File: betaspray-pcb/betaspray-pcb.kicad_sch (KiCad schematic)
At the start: 1 part, among them U1 ESP32-S3

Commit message: Add LDO
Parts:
- added U2: LM3940IT-3.3, LM3940IT-3.3:TO254P1054X470X1955-3, symbol betaspray_LDO:LM3940IT-3.3
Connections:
- net GND: now also U2.2 (GND)
- new net VDD33: U2.3 (OUT)
- new net VDD5V: U2.1 (IN)
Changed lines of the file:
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@@
+		)
+	)
+	(wire
+		(pts
+			(xy 74.93 143.51) (xy 74.93 151.13)
+		)
+		(stroke
+			(width 0)
+			(type default)
+		)
+	)
+	(wire
+		(pts
+			(xy 110.49 143.51) (xy 110.49 151.13)
+		)
+		(stroke
+			(width 0)
+			(type default)
+		)
+	)
+	(wire
+		(pts
+			(xy 110.49 156.21) (xy 110.49 161.29)
+		)
+		(stroke
+			(width 0)
+			(type default)
+		)
+	)
+	(label "VDD33"
+		(at 110.49 143.51 0)
+		(effects
+			(font
+				(size 1.27 1.27)
+			)
+			(justify left bottom)
+		)
+	)
+	(label "VDD5V"
+		(at 74.93 143.51 180)
+		(effects
+			(font
+				(size 1.27 1.27)
+			)
+			(justify right bottom)
+		)
+	)
+	(symbol
+		(lib_id "betaspray_LDO:LM3940IT-3.3")
+		(at 92.71 153.67 0)
+		(unit 1)
+		(exclude_from_sim no)
+		(in_bom yes)
+		(on_board yes)
+		(dnp no)
+		(fields_autoplaced yes)
+		(property "Reference" "U2"
+			(at 92.71 143.51 0)
+			(effects
+				(font
+					(size 1.27 1.27)
+				)
+			)
+		)
+		(property "Value" "LM3940IT-3.3"
+			(at 92.71 146.05 0)
+			(effects
+				(font
+					(size 1.27 1.27)
+				)
+			)
+		)
+		(property "Footprint" "LM3940IT-3.3:TO254P1054X470X1955-3"
+			(at 92.71 153.67 0)
+			(effects
+				(font
+					(size 1.27 1.27)
+				)
+				(justify bottom)
+				(hide yes)
+			)
+		)
+		(property "Datasheet" ""
+			(at 92.71 153.67 0)
+			(effects
+				(font
+					(size 1.27 1.27)
+				)
+				(hide yes)
+			)
+		)
+		(property "Description" ""
+			(at 92.71 153.67 0)
+			(effects
+				(font
+					(size 1.27 1.27)
+				)
+				(hide yes)
+			)
+		)
+		(pin "3"
+		)
+		(pin "2"
+		)
+		(pin "1"
+		)
+		(instances
+			(project ""
+				(path "/5d34c70f-469d-43be-b671-484e3b695429"
+					(reference "U2")
+					(unit 1)
+				)
+			)
 		)
 	)
 	(symbol
 		(lib_id "power:GND")
+		(at 110.49 161.29 0)
+		(unit 1)
+		(exclude_from_sim no)
+		(in_bom yes)
+		(on_board yes)
+		(dnp no)
+		(fields_autoplaced yes)
+		(property "Reference" "#PWR02"
+			(at 110.49 167.64 0)
+			(effects
+				(font
+					(size 1.27 1.27)
+				)
+				(hide yes)
+			)
+		)
+		(property "Value" "GND"
+			(at 110.49 166.37 0)
+			(effects
+				(font
+					(size 1.27 1.27)
+				)
+			)
+		)
+		(property "Footprint" ""
+			(at 110.49 161.29 0)
+			(effects
+				(font
+					(size 1.27 1.27)
+				)
+				(hide yes)
+			)
+		)
+		(property "Datasheet" ""
+			(at 110.49 161.29 0)
+			(effects
+				(font
+					(size 1.27 1.27)
+				)
+				(hide yes)
+			)
+		)
+		(property "Description" "Power symbol creates a global label with name \"GND\" , ground"
+			(at 110.49 161.29 0)
+			(effects
+				(font
+					(size 1.27 1.27)
+				)
+				(hide yes)
+			)
+		)
+		(pin "1"
+		)
+		(instances
+			(project ""
+				(path "/5d34c70f-469d-43be-b671-484e3b695429"
+					(reference "#PWR02")
+					(unit 1)
+				)
+			)
+		)
+	)
+	(symbol
+		(lib_id "power:GND")

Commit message: add servo control
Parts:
- added J1, J2, J3, J4, J5, J6, J7, J9: Conn_01x03_Pin, symbol betaspray_Connector:Conn_01x03_Pin
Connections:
- net GND: now also J1.1 (Pin_1), J2.1 (Pin_1), J3.1 (Pin_1), J4.1 (Pin_1), J5.1 (Pin_1), J6.1 (Pin_1), J7.1 (Pin_1), J9.1 (Pin_1)
- net VDD33: now also J1.2 (Pin_2), J2.2 (Pin_2), J3.2 (Pin_2), J4.2 (Pin_2), J5.2 (Pin_2), J6.2 (Pin_2), J7.2 (Pin_2), J9.2 (Pin_2)
- net SERV4: now reaches U1.10 (GPIO5)
- net SERV4: now also J5.3 (Pin_3)
- net SERV5: now reaches U1.11 (GPIO6)
- net SERV5: now also J6.3 (Pin_3)
- net SERV6: now reaches U1.12 (GPIO7)
- net SERV6: now also J7.3 (Pin_3)
- net SERV7: now reaches U1.13 (GPIO8)
- net SERV7: now also J9.3 (Pin_3)
- net SERV0: now reaches U1.6 (GPIO1)
- net SERV0: now also J1.3 (Pin_3)
- net SERV1: now reaches U1.7 (GPIO2)
- net SERV1: now also J2.3 (Pin_3)
- net SERV2: now reaches U1.8 (GPIO3)
- net SERV2: now also J3.3 (Pin_3)
- net SERV3: now reaches U1.9 (GPIO4)
- net SERV3: now also J4.3 (Pin_3)

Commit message: Vision subsystem sheet
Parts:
- U1: symbol betaspray_MCU_Espressif:ESP32-S3 -> betaspray_Connector:ESP32-S3
- U2: symbol betaspray_LDO:LM3940IT-3.3 -> betaspray_Connector:LM3940IT-3.3
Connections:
- no-connect marks 0 -> 1
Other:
- added sheet vision_subsystem (vision.kicad_sch)

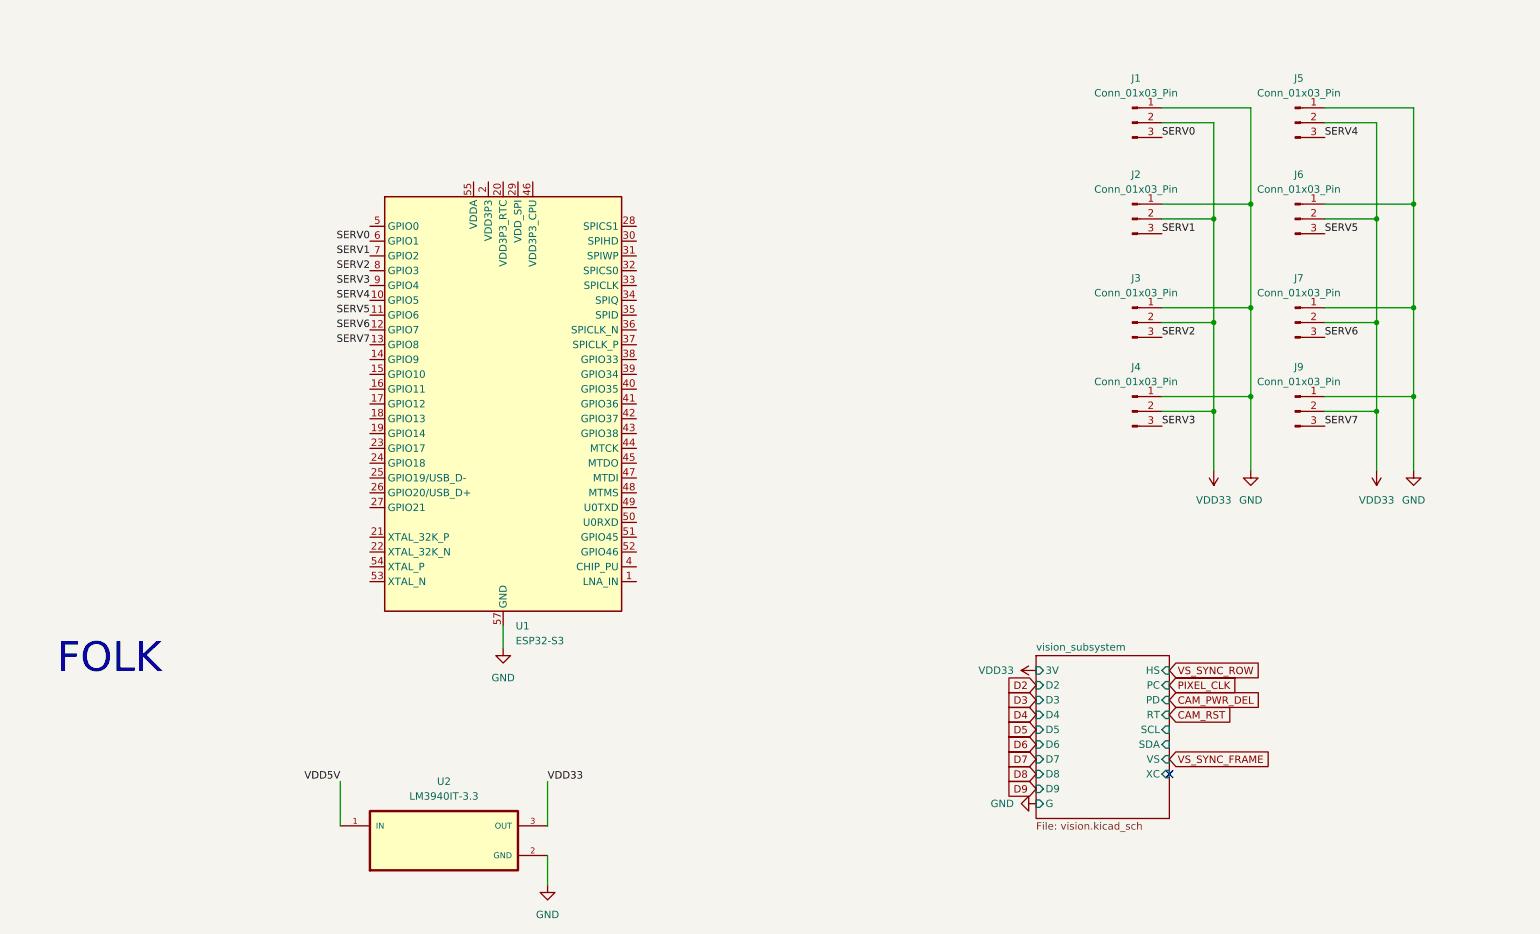
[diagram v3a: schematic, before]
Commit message: Add power sheet, fix MCU footprint?
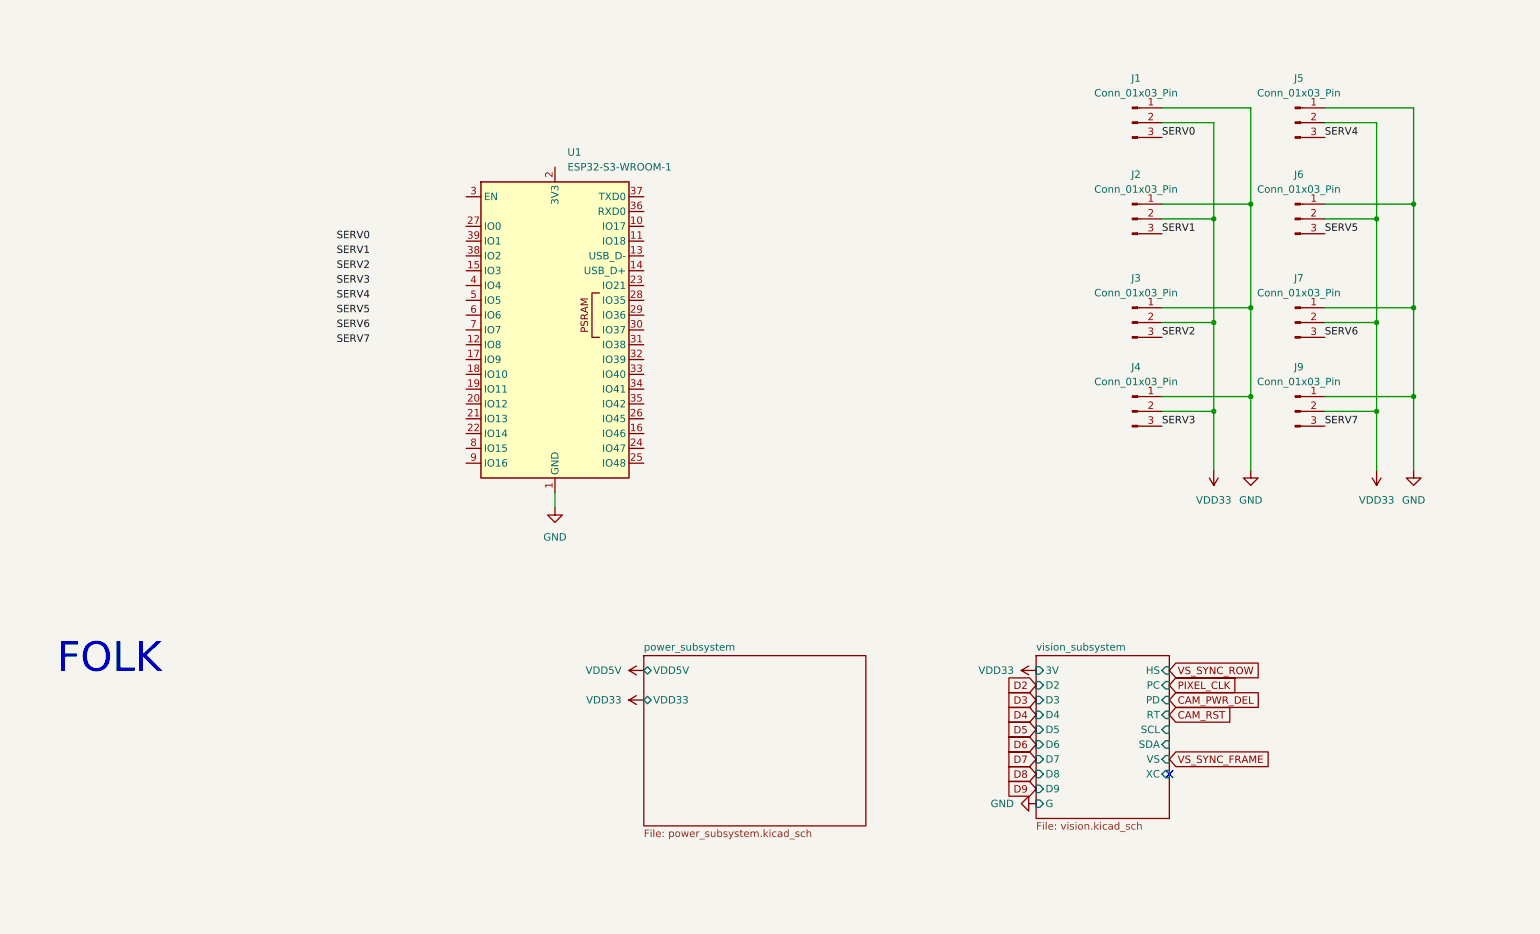
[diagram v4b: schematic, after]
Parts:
- removed U1: ESP32-S3, Package_DFN_QFN:QFN-56-1EP_7x7mm_P0.4mm_EP4x4mm, symbol betaspray_Connector:ESP32-S3
- removed U2: LM3940IT-3.3, LM3940IT-3.3:TO254P1054X470X1955-3, symbol betaspray_Connector:LM3940IT-3.3
- added U1: ESP32-S3-WROOM-1, RF_Module:ESP32-S3-WROOM-1U, symbol betaspray_MCU_Espressif:ESP32-S3-WROOM-1
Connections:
- net GND: now also U1.1 (GND), U1.40 (GND), U1.41 (GND)
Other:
- added sheet power_subsystem (power_subsystem.kicad_sch)

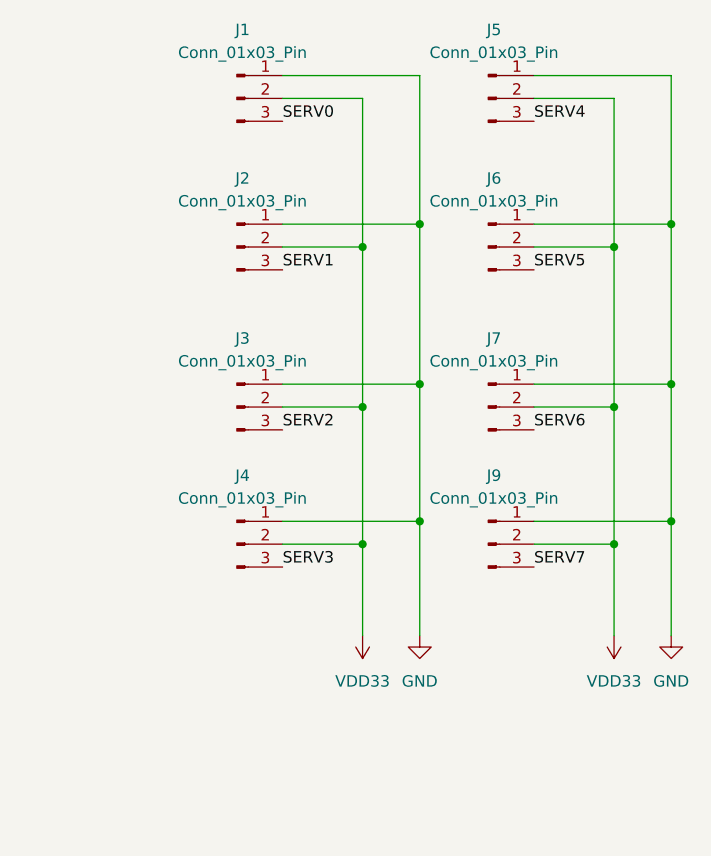
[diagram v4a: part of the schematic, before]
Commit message: add servo_subsystem
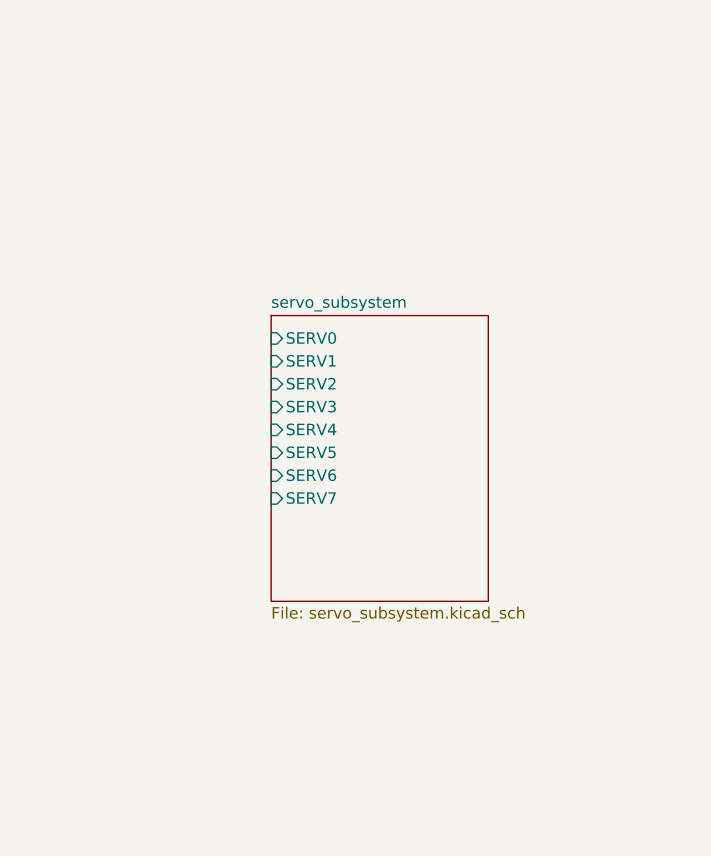
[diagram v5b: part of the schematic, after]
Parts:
- removed J1, J2, J3, J4, J5, J6, J7, J9: Conn_01x03_Pin, symbol betaspray_Connector:Conn_01x03_Pin
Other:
- added sheet servo_subsystem (servo_subsystem.kicad_sch)

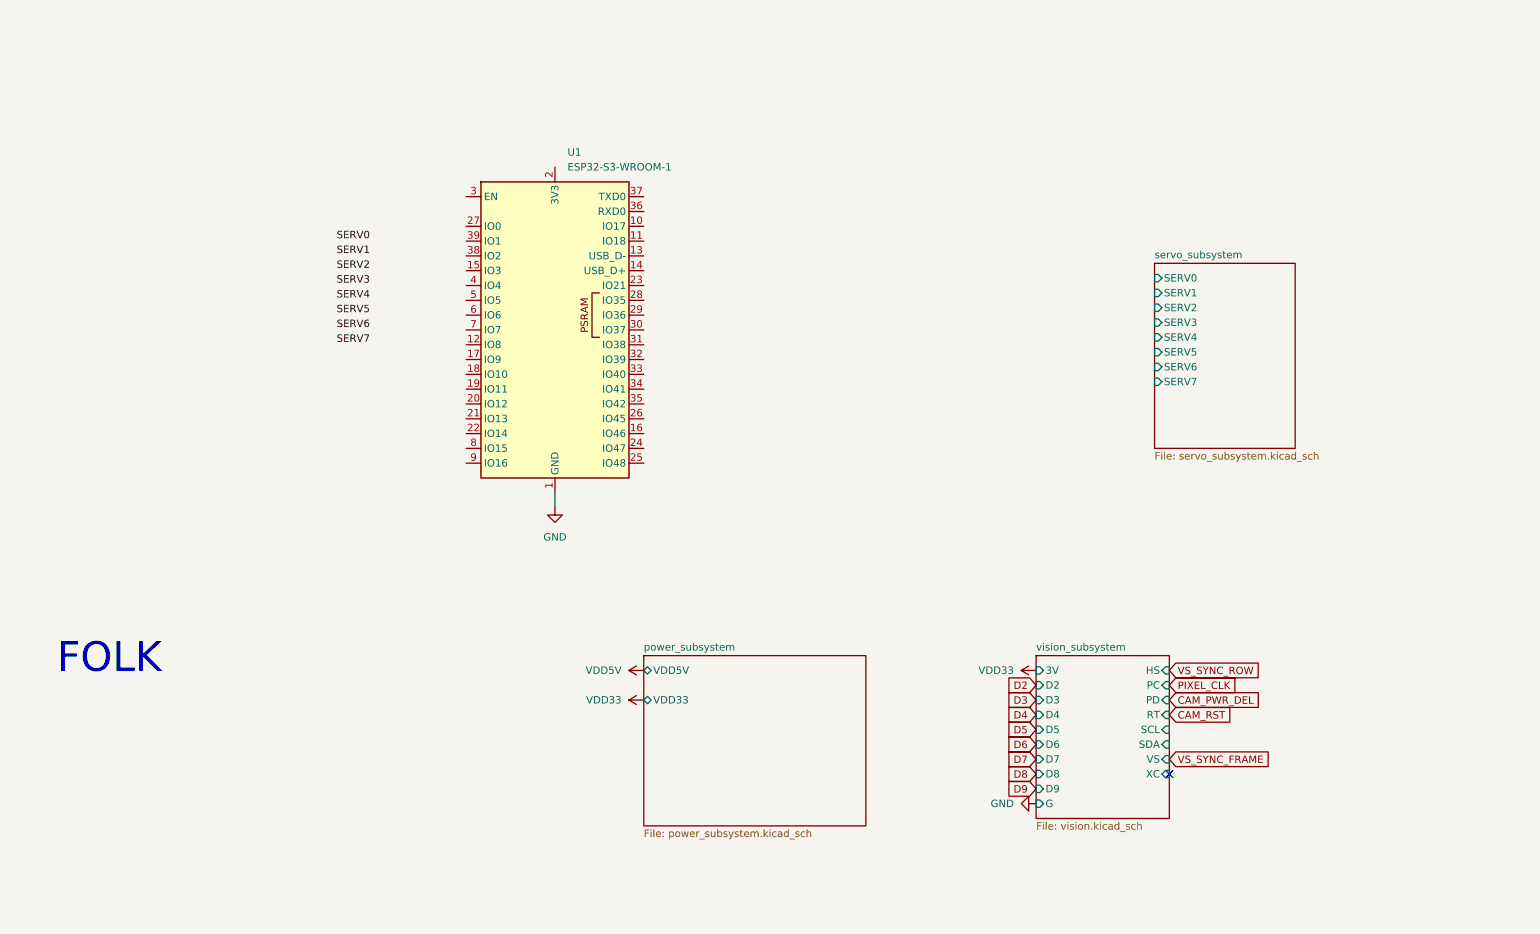
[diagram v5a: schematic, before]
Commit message: Add USB-C, connection, power decoupling
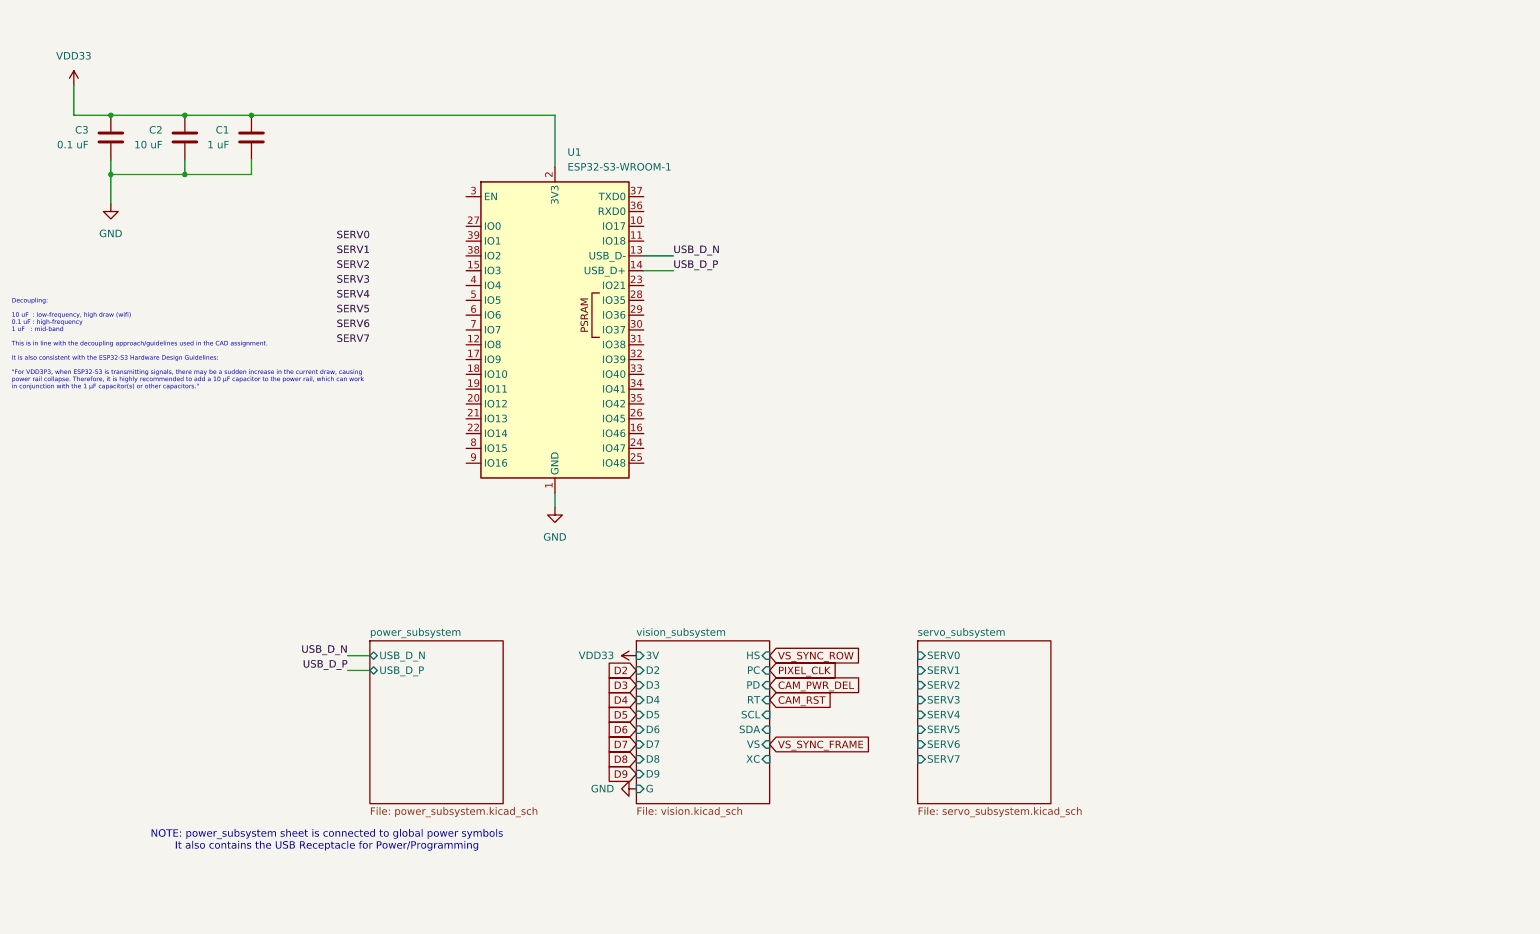
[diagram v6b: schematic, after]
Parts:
- added C1: 1 uF, symbol betaspray_LDO:C
- added C2: 10 uF, symbol betaspray_LDO:C
- added C3: 0.1 uF, symbol Device:C
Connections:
- net GND: now also C1.2, C2.2, C3.2
- net VDD33: now also U1.2 (3V3), C1.1, C2.1, C3.1
- net USB_D_N: now reaches U1.13 (USB_D-)
- net USB_D_P: now reaches U1.14 (USB_D+)
- no-connect marks 1 -> 0
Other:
- sheet power_subsystem ports: added USB_D_N, USB_D_P; removed VDD33, VDD5V
- note added: "Decoupling: 10 uF : low-frequency, high draw (wifi) 0.1 uF : high-frequency 1 uF : mid-band This is in line with the decoupling approach/guidelines used in the CAD assignment. It is also consistent with the ESP32-S3 Hardware Design Guidelines: "For VDD3P3, when ESP32-S3 is transmitting signals, there may be a sudden increase in the current draw, causing power rail collapse. Therefore, it is highl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"
- note added: "NOTE: power_subsystem sheet is connected to global power symbols It also contains the USB Receptacle for Power/Programming"
- note removed: "FOLK"
